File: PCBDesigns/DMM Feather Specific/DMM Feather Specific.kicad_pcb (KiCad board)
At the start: 4 copper layers, 68.5 x 53.2 mm, 58 parts, among them J10 I_Input, J11 Conn_01x02_Pin, J13 Conn_01x16_Socket, J14 Conn_01x12_Socket, J4 Out to Screen, J7 Barrel_Jack, J8 Conn_01x01_Socket, J9 Barrel_Jack, Q1 MMBT3904, Q2 AO3400A MOSFET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

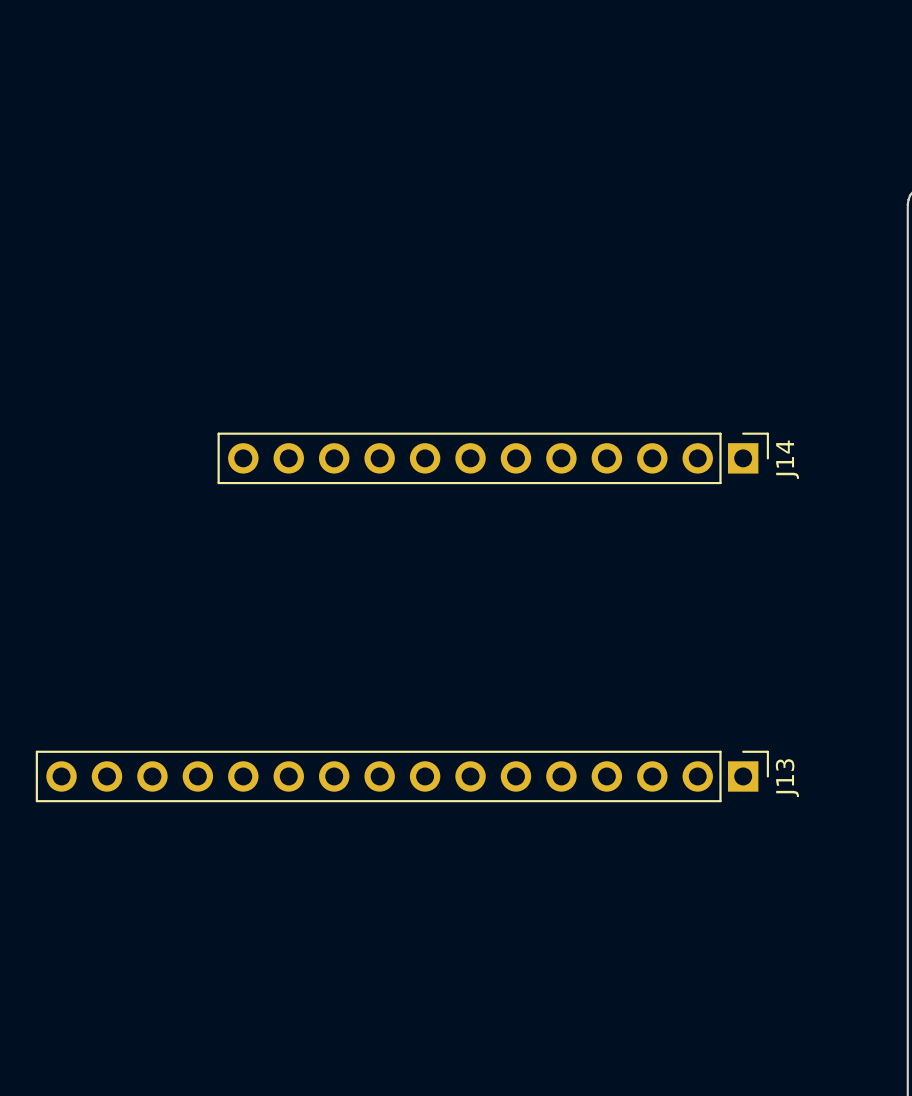
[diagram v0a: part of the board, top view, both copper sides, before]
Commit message: Updates, see description
Updated programming for open lead detect board
worked on various PCBs, including a new open lead voltmeter design with few components
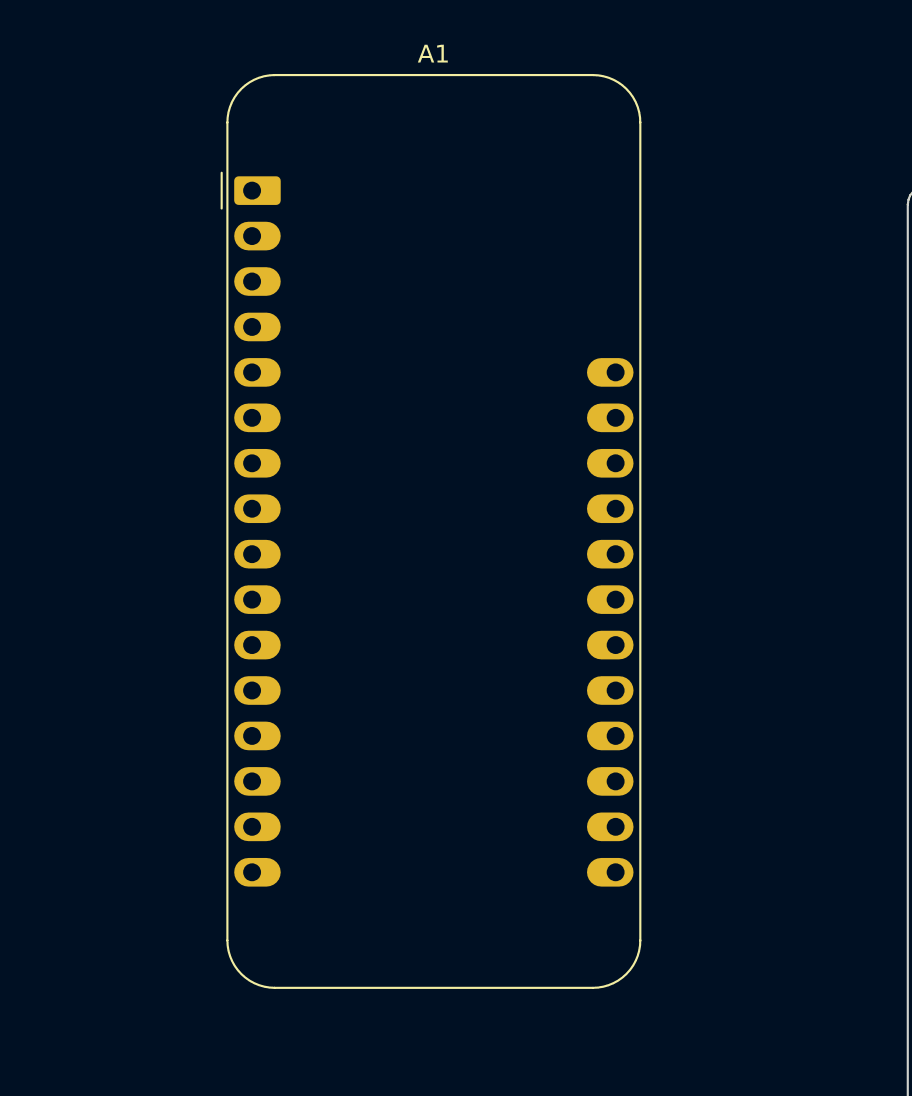
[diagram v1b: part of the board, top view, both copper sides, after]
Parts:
- removed J13: Conn_01x16_Socket, Connector_PinHeader_2.54mm:PinHeader_1x16_P2.54mm_Vertical
- removed J14: Conn_01x12_Socket, Connector_PinHeader_2.54mm:PinHeader_1x12_P2.54mm_Vertical
- added A1: Adafruit_Feather_Generic, Module:Adafruit_Feather, F.Cu at (41.8, 48.5)
